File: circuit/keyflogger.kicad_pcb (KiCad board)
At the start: 2 copper layers, 45 x 19 mm, 18 parts, among them J1 USB_A, J2 Conn_PIC_ICSP_ICD, J3 USB_B_Micro, Q1 2N7002, Q2 2N7002, Q3 2N7002, Q4 2N7002, U1 PIC16F1454-IP, U2 PIC16F1454-IP

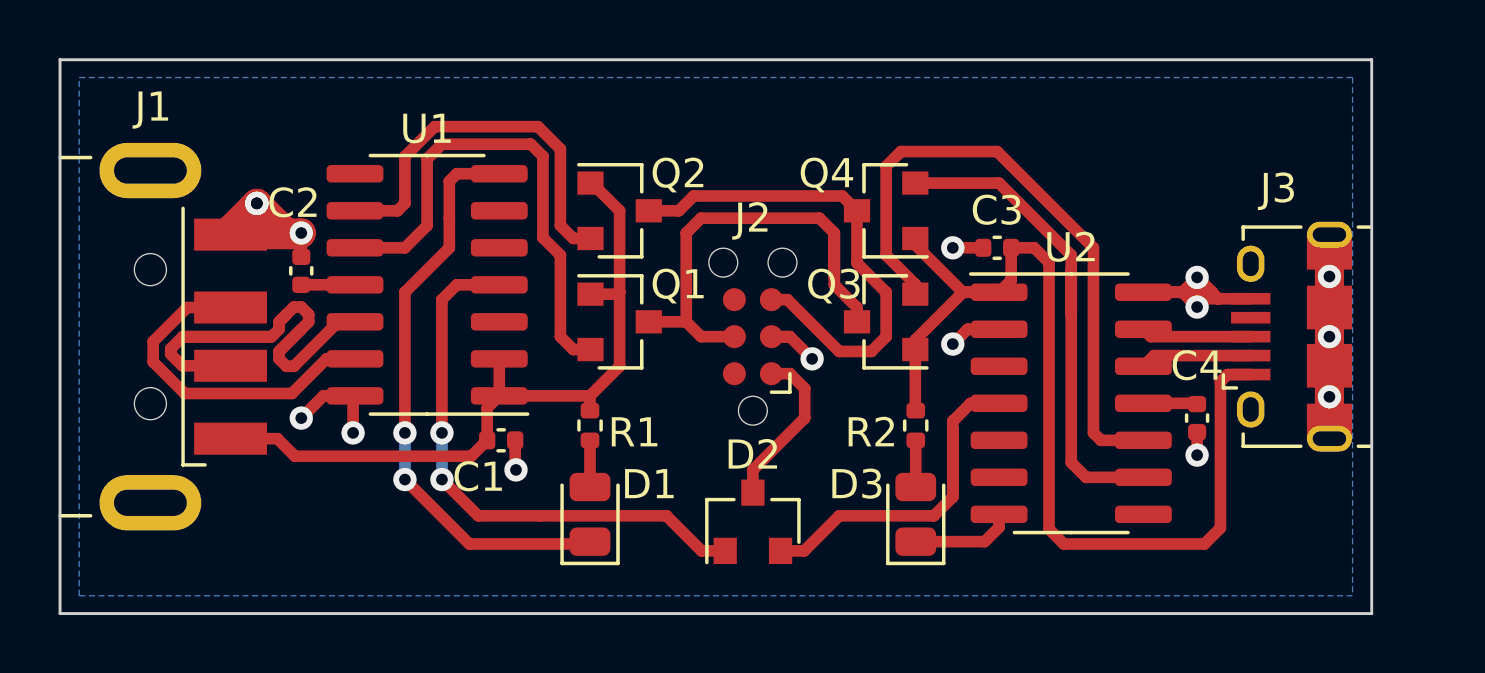
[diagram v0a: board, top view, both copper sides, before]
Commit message: circuit: Add 1M resistors to prevent VDDx from floating
Ensure that the I2C MOSFET gates are not left floating (and hence
potentially failing to isolate) when power is disconnected.

Signed-off-by: Michael Brown <mbrown@fensystems.co.uk>
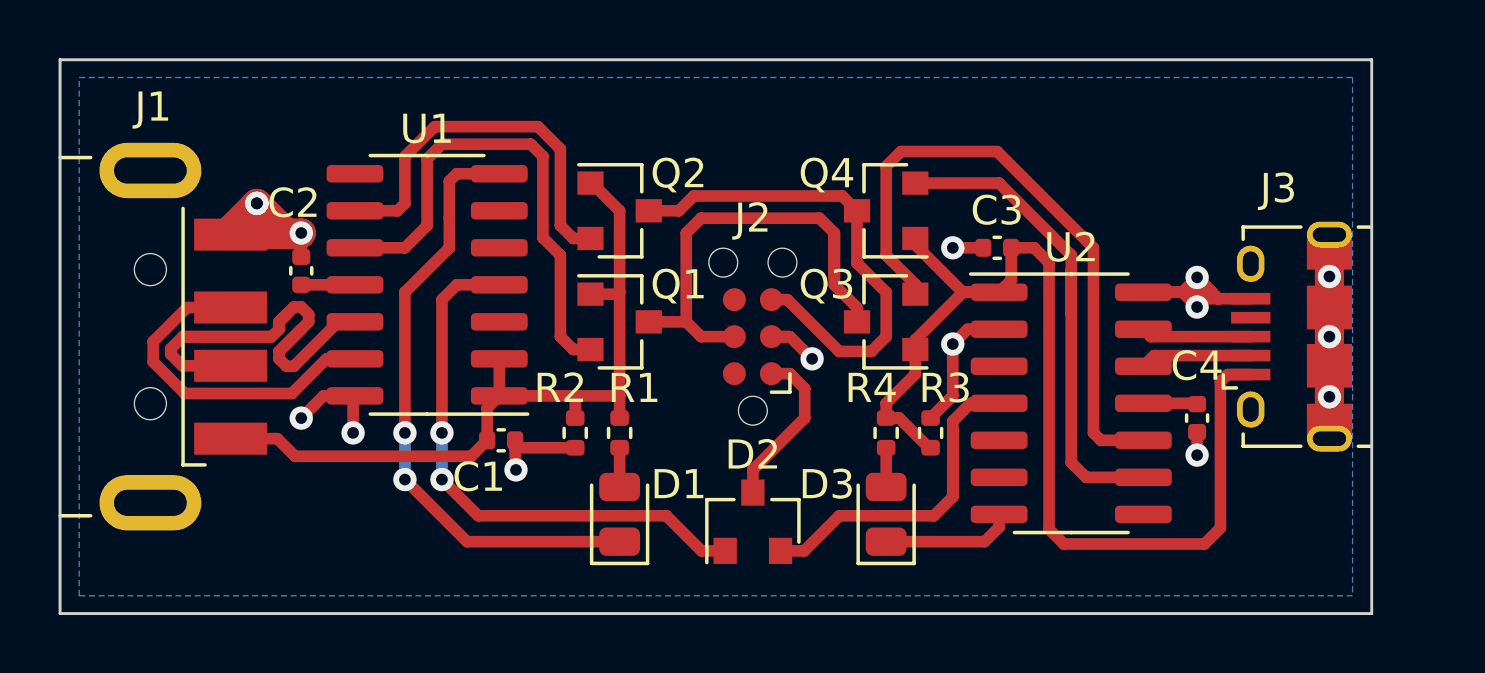
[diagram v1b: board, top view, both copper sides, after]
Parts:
- added R2: 1M, Resistor_SMD:R_0402_1005Metric, F.Cu at (150.1, 107.4)
- added R3: 1M, Resistor_SMD:R_0402_1005Metric, F.Cu at (162.3, 107.4)
- moved R1 1.05 mm to (151.6, 107.4)
- moved R4 1.05 mm to (160.8, 107.4)
- moved D1 1.02 mm to (151.6, 110.2)
- moved D3 1.02 mm to (160.8, 110.2)
- renumbered R2 to R4
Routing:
- net GND: track 33.9 -> 38.8 mm
- net VDD2: track 34.8 -> 37.4 mm
- net VDD1: track 25.1 -> 26.7 mm
- net /STATUS2: track 3.51 -> 4.52 mm
- net /STATUS1: track 20.0 -> 20.9 mm

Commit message: circuit: Use two separate ICSP connectors
Programming two (identical) PICs in parallel via a single ICSP
connector does work.  However, the requirement to avoid back powering
via the nMCLR/VPP pin is cumbersome to overcome: high-voltage
programming requires the programmer to be able to drive nMCLR/VPP to
at least 8.0V (thereby preventing the use of a common cathode diode)
while low-voltage programming requires the programmer to be able to
pull nMCLR/VPP down to 0V (thereby preventing the use of a common
anode diode).

Split out a separate ICSP connector for each PIC.  Since there are now
separate VDD pins for each ICSP connector, the VDD pins may now be
connected to VDD1/VDD2, thereby allowing the programmer to power the
PIC during programming (rather than requiring USB power).

Remove the identification strapping pin, since there is no longer a
requirement for each PIC to contain identical firmware.

Drive the I2C enable from an I/O pin (rather than directly from
VDD1/VDD2), to ensure that each PIC is automatically isolated from the
I2C bus while programming is in progress.

Signed-off-by: Michael Brown <mbrown@fensystems.co.uk>
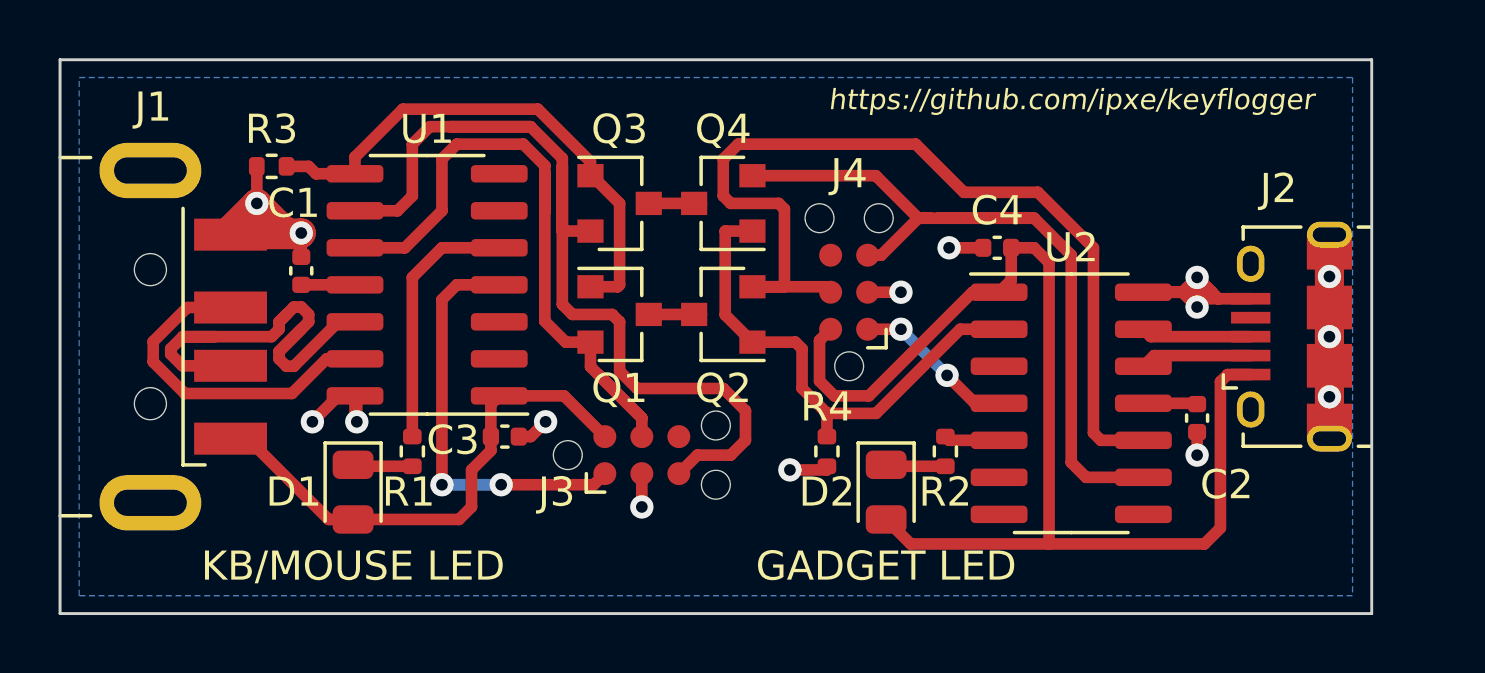
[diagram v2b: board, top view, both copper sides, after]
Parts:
- removed the C4 at (171.4, 106.9)
- removed D3: LED, LED_SMD:LED_0805_2012Metric
- removed the R4 at (160.8, 107.4)
- added C2: 470n, Capacitor_SMD:C_0402_1005Metric, F.Cu at (171.4, 106.9)
- added J4: Conn_PIC_ICSP_ICD, Connector:Tag-Connect_TC2030-IDC-NL_2x03_P1.27mm_Vertical, F.Cu at (159.5, 102.6)
- added R3: 1M, Resistor_SMD:R_0402_1005Metric, F.Cu at (139.7, 98.3)
- D2: value BAT54C -> LED; footprint Package_TO_SOT_SMD:SOT-23 -> LED_SMD:LED_0805_2012Metric
- R2: value 1M -> 1K5
- moved R2 12.7 mm to (162.8, 108.1), turned to 90 degrees
- moved Q3 10.0 mm to (151.6, 99.6), turned to 0 degrees
- moved D1 9.18 mm to (142.5, 109.5), turned to 270 degrees
- moved R1 7.14 mm to (144.5, 108.1), turned to 90 degrees
- moved Q4 5.59 mm to (155.2, 99.6)
- moved J3 5.57 mm to (152.4, 108.2), turned to 0 degrees
- moved Q2 5.03 mm to (155.2, 103.4), turned to 180 degrees
- moved D2 4.68 mm to (160.8, 109.5), turned to 270 degrees
- moved R4 3.61 mm to (158.8, 108.1), turned to 270 degrees
- moved Q1 0.25 mm to (151.6, 103.4)
- moved C3 0.18 mm to (147.7, 107.6)
- renumbered C2 to C1, C1 to C3, C3 to C4, J3 to J2, J2 to J3, R3 to R4
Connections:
- net /SDA_ICSPCLK_2 renamed /SDA_ICSPCLK2
- net Net-(C2-Pad1) renamed /VUSB1
- D1 pad 1: /STATUS1 -> Net-(D1-Pad1)
- D1 pad 2: Net-(D1-Pad2) -> VDD1
- D2 pad 1: /~MCLR1~ -> Net-(D2-Pad1)
- D2 pad 2: /~MCLR2~ -> VDD2
- J3 pad 1: /~MCLR~ -> /~MCLR~_VPP1
- J3 pad 2: (no net) -> VDD1
- J3 pad 4: /SCL_ICSPDAT -> /SCL_ICSPDAT1
- J3 pad 5: /SDA_ICSPCLK -> /SDA_ICSPCLK1
- Q1 pad 1: VDD1 -> /I2C_EN1
- Q1 pad 2: /SCL_ICSPDAT_1 -> /SCL_ICSPDAT1
- Q1 pad 3: /SCL_ICSPDAT -> /SCL
- Q2 pad 1: VDD1 -> /I2C_EN2
- Q2 pad 2: /SDA_ICSPCLK_1 -> /SCL_ICSPDAT2
- Q2 pad 3: /SDA_ICSPCLK -> /SCL
- Q3 pad 1: VDD2 -> /I2C_EN1
- Q3 pad 2: /SCL_ICSPDAT_2 -> /SDA_ICSPCLK1
- Q3 pad 3: /SCL_ICSPDAT -> /SDA
- Q4 pad 1: VDD2 -> /I2C_EN2
- Q4 pad 3: /SDA_ICSPCLK -> /SDA
- R1 pad 1: VDD1 -> Net-(D1-Pad1)
- R1 pad 2: Net-(D1-Pad2) -> /LED1
- R2 pad 1: VDD1 -> Net-(D2-Pad1)
- R2 pad 2: GND -> /LED2
- R4 pad 1: VDD2 -> /I2C_EN2
- U1 pad 10: /SCL_ICSPDAT_1 -> /SCL_ICSPDAT1
- U1 pad 2: VDD1 -> (no net)
- U1 pad 4: /~MCLR1~ -> /~MCLR~_VPP1
- U1 pad 5: (no net) -> /LED1
- U1 pad 7: /STATUS1 -> (no net)
- U1 pad 8: (no net) -> /I2C_EN1
- U1 pad 9: /SDA_ICSPCLK_1 -> /SDA_ICSPCLK1
- U2 pad 10: /SCL_ICSPDAT_2 -> /SCL_ICSPDAT2
- U2 pad 11: Net-(C4-Pad1) -> /VUSB2
- U2 pad 2: GND -> /I2C_EN2
- U2 pad 4: /~MCLR2~ -> /~MCLR~_VPP2
- U2 pad 5: (no net) -> /LED2
- U2 pad 7: /STATUS2 -> (no net)
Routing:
- net /SDA_ICSPCLK1: track 0.00 -> 33.4 mm
- net /SCL_ICSPDAT2: track 0.00 -> 32.6 mm
- net /SCL_ICSPDAT1: track 0.00 -> 24.0 mm
- net /SCL_ICSPDAT_2: track 21.7 -> 0.00 mm
- net /STATUS1: track 20.9 -> 0.00 mm, vias 2 -> 0
- net /~MCLR1~: track 19.1 -> 0.00 mm, vias 2 -> 0
- net /I2C_EN1: track 0.00 -> 18.2 mm
- net /I2C_EN2: track 0.00 -> 17.4 mm
- net /SDA_ICSPCLK: track 17.2 -> 0.00 mm
- net /SCL_ICSPDAT_1: track 17.1 -> 0.00 mm
- net /SCL_ICSPDAT: track 16.6 -> 0.00 mm
- net /~MCLR~_VPP1: track 0.00 -> 14.3 mm, vias 0 -> 2
- net /~MCLR2~: track 13.5 -> 0.00 mm
- net /SDA_ICSPCLK_1: track 13.4 -> 0.00 mm
- net /SDA_ICSPCLK2: track 17.7 -> 27.9 mm
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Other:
- board text added: "GADGET LED"
- board text added: "KB/MOUSE LED"
- board text added: "https://github.com/ipxe/keyflogger"

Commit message: circuit: Add front ground plane
Signed-off-by: Michael Brown <mbrown@fensystems.co.uk>
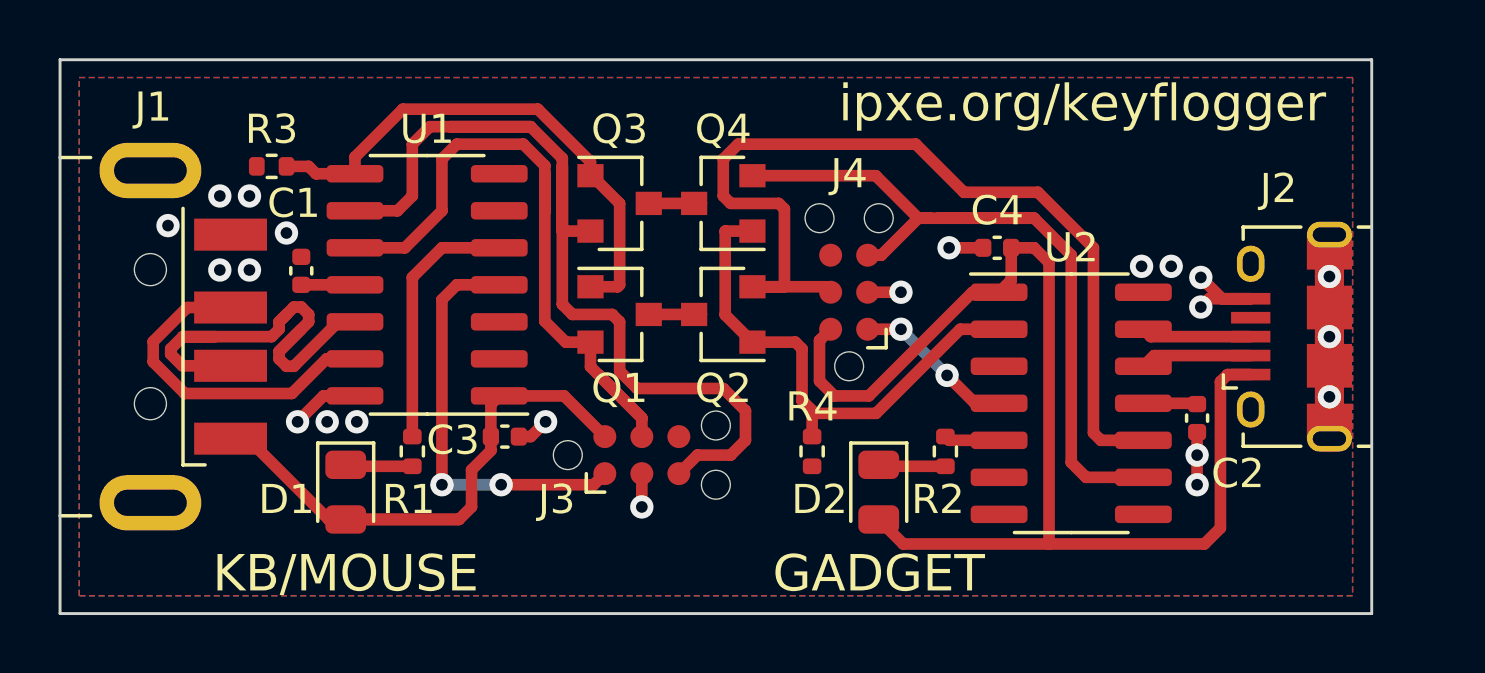
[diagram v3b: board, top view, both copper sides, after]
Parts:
- moved R4 0.51 mm to (158.2, 108.1)
- moved D2 0.25 mm to (160.5, 109.5)
- moved D1 0.25 mm to (142.2, 109.5)
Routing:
- net GND: track 35.3 -> 18.4 mm, vias 15 -> 22
- net VDD1: track 18.0 -> 21.6 mm
- net /I2C_EN2: track 17.4 -> 18.2 mm
- added copper zone on F.Cu, net GND
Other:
- board text added: "GADGET"
- board text added: "KB/MOUSE"
- board text added: "ipxe.org/keyflogger"
- board text removed: "GADGET LED"
- board text removed: "KB/MOUSE LED"
- board text removed: "https://github.com/ipxe/keyflogger"

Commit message: circuit: Switch to using the UART to provide the data channel
The PICs do not provide internal pull-ups on the I2C SCL/SDA pins,
which would increase the external component count for the data channel
to 10 parts in total (4x MOSFETs, 4x pull-up resistors, 2x pull-down
resistors).

Switch to using the UART, which requires only 6 external components
(2x MOSFETs, 2x pull-up resistors, 2x pull-down resistors) and has the
advantage that the data channel may be snooped (or emulated) using an
off-the-shelf USB TTL UART adapter.

Signed-off-by: Michael Brown <mbrown@fensystems.co.uk>
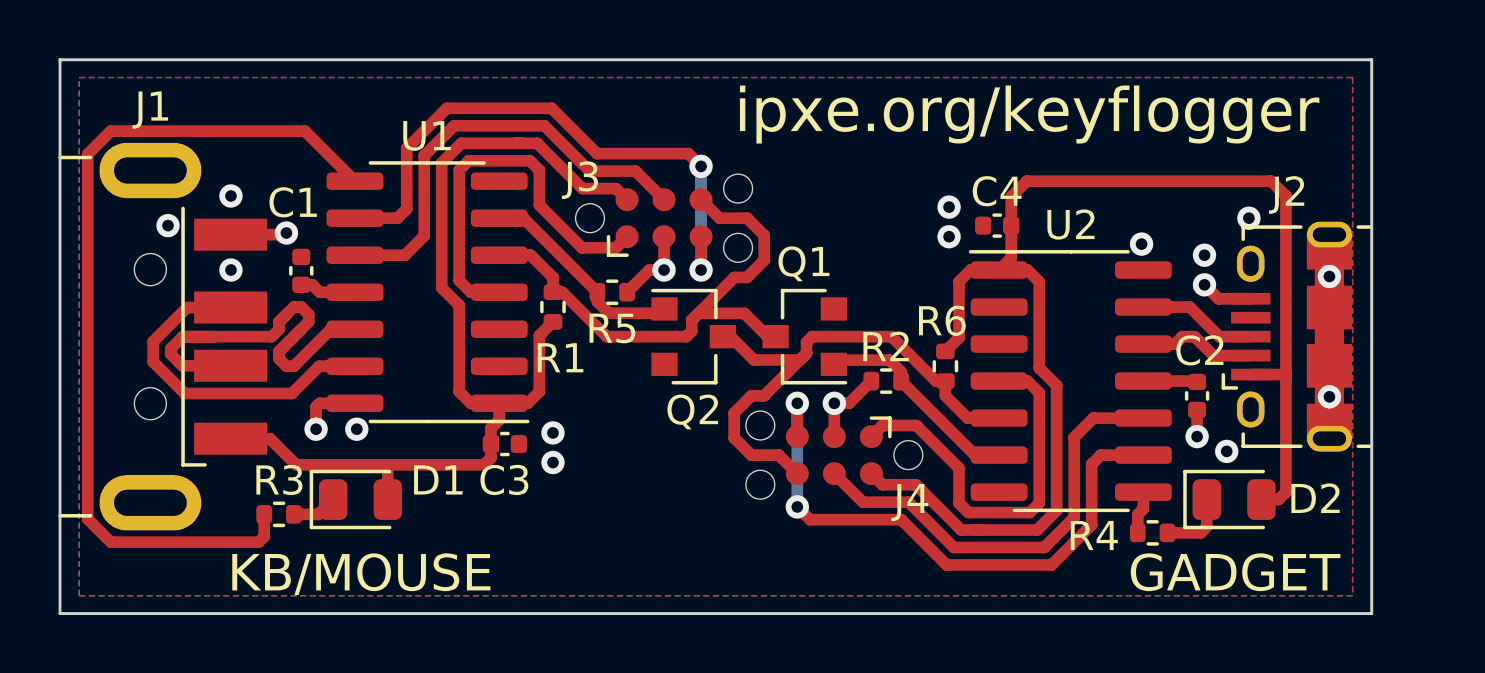
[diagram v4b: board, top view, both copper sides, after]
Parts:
- removed Q3, Q4: 2N7002, Package_TO_SOT_SMD:SOT-23
- removed the R4 at (158.2, 108.1)
- added R3: 1K5, Resistor_SMD:R_0402_1005Metric, F.Cu at (140.0, 110.2)
- added R5: 4K7, Resistor_SMD:R_0402_1005Metric, F.Cu at (151.4, 102.6)
- added R6: 4K7, Resistor_SMD:R_0402_1005Metric, F.Cu at (162.8, 105.2)
- R1: value 1K5 -> 4K7
- R2: renamed from R3; value 1M -> 4K7
- moved R2 22.3 mm to (160.8, 105.7)
- moved D2 12.2 mm to (172.7, 109.7), turned to 0 degrees
- moved J3 8.16 mm to (153.2, 100.1)
- moved R4 7.64 mm to (169.9, 110.9), turned to 180 degrees
- moved R1 6.92 mm to (149.4, 103.1), turned to 270 degrees
- moved Q1 6.40 mm to (158.0, 104.1), turned to 180 degrees
- moved J4 5.61 mm to (159.0, 108.2), turned to 180 degrees
- moved Q2 1.27 mm to (154.2, 104.1), turned to 0 degrees
- moved C2 0.76 mm to (171.4, 106.2)
- moved C4 0.76 mm to (164.6, 100.3)
- moved U2 0.76 mm to (167.1, 105.7)
- moved D1 0.57 mm to (142.7, 109.7), turned to 0 degrees
- moved U1 0.25 mm to (145.0, 102.6)
- moved C3 0.25 mm to (147.7, 107.8)
- renumbered R2 to R4
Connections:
- net /SDA_ICSPCLK1 renamed /ICSPCLK1
- net /SDA_ICSPCLK2 renamed /ICSPCLK2
- J3 pad 4: /SCL_ICSPDAT1 -> /ICSPDAT1
- J3 pad 6: (no net) -> /RX1
- J4 pad 4: /SCL_ICSPDAT2 -> /ICSPDAT2
- J4 pad 6: (no net) -> /RX2
- Q1 pad 1: /I2C_EN1 -> /~TX2~
- Q1 pad 2: /SCL_ICSPDAT1 -> GND
- Q1 pad 3: /SCL -> /RX1
- Q2 pad 1: /I2C_EN2 -> /~TX1~
- Q2 pad 2: /SCL_ICSPDAT2 -> GND
- Q2 pad 3: /SCL -> /RX2
- R1 pad 1: Net-(D1-Pad1) -> /RX1
- R1 pad 2: /LED1 -> VDD1
- R2 pad 1: /I2C_EN1 -> /~TX2~
- R4 pad 2: /LED2 -> /~LED2~
- U1 pad 10: /SCL_ICSPDAT1 -> /ICSPDAT1
- U1 pad 5: /LED1 -> /RX1
- U1 pad 6: (no net) -> /~TX1~
- U1 pad 8: /I2C_EN1 -> /~LED1~
- U2 pad 10: /SCL_ICSPDAT2 -> /ICSPDAT2
- U2 pad 2: /I2C_EN2 -> (no net)
- U2 pad 5: /LED2 -> /RX2
- U2 pad 6: (no net) -> /~TX2~
- U2 pad 8: (no net) -> /~LED2~
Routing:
- net /SCL_ICSPDAT2: track 32.6 -> 0.00 mm
- net /~LED1~: track 0.00 -> 30.0 mm
- net /SCL_ICSPDAT1: track 24.0 -> 0.00 mm
- net /RX2: track 0.00 -> 18.7 mm
- net /RX1: track 0.00 -> 18.7 mm
- net /I2C_EN1: track 18.2 -> 0.00 mm
- net /I2C_EN2: track 18.2 -> 0.00 mm
- net /ICSPDAT1: track 0.00 -> 15.1 mm
- net /ICSPDAT2: track 0.00 -> 15.1 mm
- net /ICSPCLK1: track 33.4 -> 20.3 mm, vias 0 -> 2
- net VDD1: track 21.6 -> 34.3 mm
- net /LED1: track 8.86 -> 0.00 mm
- net /~MCLR~_VPP2: track 5.56 -> 13.3 mm, vias 2 -> 0
- net /ICSPCLK2: track 27.9 -> 20.3 mm, vias 0 -> 2
- net /~TX1~: track 0.00 -> 7.27 mm
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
